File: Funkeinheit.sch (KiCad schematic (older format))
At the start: 3 parts, among them IC1 74HC4050

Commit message: Implements stepup dc/dc
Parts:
- removed IC1: 74HC4050, Housings_SSOP:SSOP-16_5.3x6.2mm_Pitch0.65mm, symbol 74HC4050
- added C10: 220nF, symbol C
- added C11: 100nF, symbol C
- added C12, C13, C7, C8: 150uF, symbol CP
- added C9: 10nF, symbol C
- added D2: D_Schottky, symbol D_Schottky
- added L2: 1uH, symbol L
- added Q1, Q2, Q3, Q4, Q5: Q_NPN_BCE, symbol Q_NPN_BCE
- added Q6: Q_NPN_BCE, TO_SOT_Packages_SMD:TSOT-23_HandSoldering, symbol Q_NPN_BCE
- added R10, R11, R12, R13, R9: 4k7, symbol R
- added R14, R15, R16, R17, R18, R4, R5, R6, R7, R8: 10k, symbol R
- added R19, R20: 100k, symbol R
- added R21: 35k, symbol R
- added R22, R23: 270k, symbol R
- added R24: 2R, symbol R
- added U2: MAX1709, Housings_SSOP:TSSOP-28-1EP_4.4x9.7mm_Pitch0.65mm, symbol MAX1709
- R2: value R -> 10k
- R3: value R -> 4k7
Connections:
- net labels added: +5V, 5V, PGND, ~ENABLE~
- wire segments 13 -> 78
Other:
- note added: "ESR < 15mOhm\nPolymer Capacitor"
- note added: "I > 1.5A\nf = 600kHz"
- note added: "Low ESR Tantal"
- note added: "Pmax > 500mW"

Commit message: Adds new Modules and WDT Circuit
- Added Schematic for MAX892 Highside Switch
- Added Schematic for MC74HC4538A
- Constructed Watchdogtimer Circuit to Reset µC and Radiomodule
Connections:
- wire segments 78 -> 80
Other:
- note added: "Ground Bridge"
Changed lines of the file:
@@
 Text Label 2850 4450 0    60   ~ 0
 MISO
-Text HLabel 2200 4800 3    60   Input ~ 0
-GND
 Text HLabel 2150 1400 0    60   Input ~ 0
 SS
@@
 	1    0    0    -1
 $EndComp
-Text HLabel 10050 1750 2    60   Input ~ 0
-GND
 $Comp
 L CP C13
@@
 	0    1    1    0
 $EndComp
-Text HLabel 5400 950  0    60   Input ~ 0
-+3.3V
 $Comp
 L CP C8
@@
 Wire Wire Line
 	3800 1400 4250 1400
-Text HLabel 8250 3150 3    60   Input ~ 0
-GND
 $Comp
 L R R23
@@
 Wire Wire Line
 	7000 1650 6700 1650
-Text HLabel 6700 2050 3    60   Input ~ 0
-GND
 $Comp
 L R R19
@@
 	1    0    0    -1
 $EndComp
-Text HLabel 6200 2150 3    60   Input ~ 0
-GND
 Wire Wire Line
 	6400 1850 6000 1850
@@
 Wire Wire Line
 	10800 2550 10800 1450
+$Comp
+L GND #PWR?
+U 1 1 59B87665
+P 2200 4800
+F 0 "#PWR?" H 2200 4550 50  0001 C CNN
+F 1 "GND" H 2200 4650 50  0000 C CNN
+F 2 "" H 2200 4800 50  0001 C CNN
+F 3 "" H 2200 4800 50  0001 C CNN
+	1    2200 4800
+	1    0    0    -1
+$EndComp
+$Comp
+L GND #PWR?
+U 1 1 59B876F0
+P 6200 2150
+F 0 "#PWR?" H 6200 1900 50  0001 C CNN
+F 1 "GND" H 6200 2000 50  0000 C CNN
+F 2 "" H 6200 2150 50  0001 C CNN
+F 3 "" H 6200 2150 50  0001 C CNN
+	1    6200 2150
+	1    0    0    -1
+$EndComp
+$Comp
+L GND #PWR?
+U 1 1 59B879C4
+P 6700 2050
+F 0 "#PWR?" H 6700 1800 50  0001 C CNN
+F 1 "GND" H 6700 1900 50  0000 C CNN
+F 2 "" H 6700 2050 50  0001 C CNN
+F 3 "" H 6700 2050 50  0001 C CNN
+	1    6700 2050
+	1    0    0    -1
+$EndComp
+$Comp
+L GND #PWR?
+U 1 1 59B87A4D
+P 8250 3150
+F 0 "#PWR?" H 8250 2900 50  0001 C CNN
+F 1 "GND" H 8250 3000 50  0000 C CNN
+F 2 "" H 8250 3150 50  0001 C CNN
+F 3 "" H 8250 3150 50  0001 C CNN
+	1    8250 3150
+	1    0    0    -1
+$EndComp
+$Comp
+L GND #PWR?
+U 1 1 59B87B99
+P 10050 1750
+F 0 "#PWR?" H 10050 1500 50  0001 C CNN
+F 1 "GND" H 10050 1600 50  0000 C CNN
+F 2 "" H 10050 1750 50  0001 C CNN
+F 3 "" H 10050 1750 50  0001 C CNN
+	1    10050 1750
+	0    -1   -1   0
+$EndComp
+Connection ~ 8250 3150
+$Comp
+L GND #PWR?
+U 1 1 59B89289
+P 4750 3700
+F 0 "#PWR?" H 4750 3450 50  0001 C CNN
+F 1 "GND" H 4750 3550 50  0000 C CNN
+F 2 "" H 4750 3700 50  0001 C CNN
+F 3 "" H 4750 3700 50  0001 C CNN
+	1    4750 3700
+	1    0    0    -1
+$EndComp
+Wire Wire Line
+	4750 3700 4750 3650
+Wire Wire Line
+	4750 3650 5550 3650
+Text Label 5550 3650 0    60   ~ 0
+PGND
+Wire Notes Line
+	4650 3500 4650 3900
+Wire Notes Line
+	4650 3900 5900 3900
+Wire Notes Line
+	5900 3900 5900 3500
+Wire Notes Line
+	5900 3500 4650 3500
+Text Notes 4700 3450 0    60   ~ 0
+Ground Bridge
 $EndSCHEMATC

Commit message: Adds ESD Protection and finalisation of wdt
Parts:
- removed C10: 220nF, symbol C
- removed C11: 100nF, symbol C
- removed C12, C13, C7, C8: 150uF, symbol CP
- removed C9: 10nF, symbol C
- removed D2: D_Schottky, symbol D_Schottky
- removed L2: 1uH, symbol L
- removed Q6: Q_NPN_BCE, TO_SOT_Packages_SMD:TSOT-23_HandSoldering, symbol Q_NPN_BCE
- removed R19, R20: 100k, symbol R
- removed R21: 35k, symbol R
- removed R22, R23: 270k, symbol R
- removed R24: 2R, symbol R
- removed U2: MAX1709, Housings_SSOP:TSSOP-28-1EP_4.4x9.7mm_Pitch0.65mm, symbol MAX1709
- added C? (x2): 47µF, symbol C
- added C?: C, symbol C
- added L?: L, symbol L
- added U?: LTC3113, symbol LTC3113
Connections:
- net labels added: VBAT
- net labels removed: +5V, ~ENABLE~
- wire segments 80 -> 52
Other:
- note removed: "ESR < 15mOhm\nPolymer Capacitor"
- note removed: "I > 1.5A\nf = 600kHz"
- note removed: "Low ESR Tantal"
- note removed: "Pmax > 500mW"

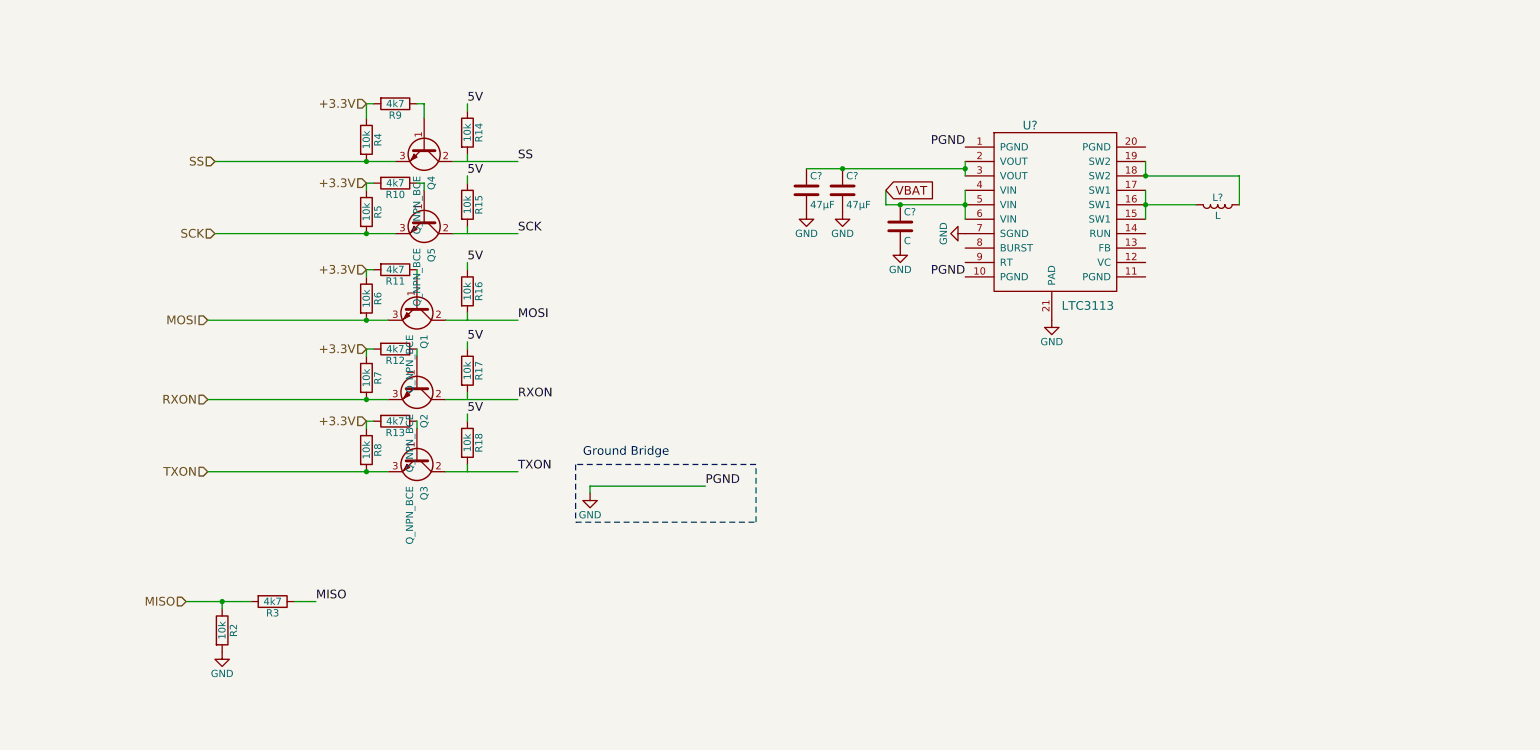
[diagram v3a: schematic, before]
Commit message: Adds RFM23BP Module to Bib and Layout
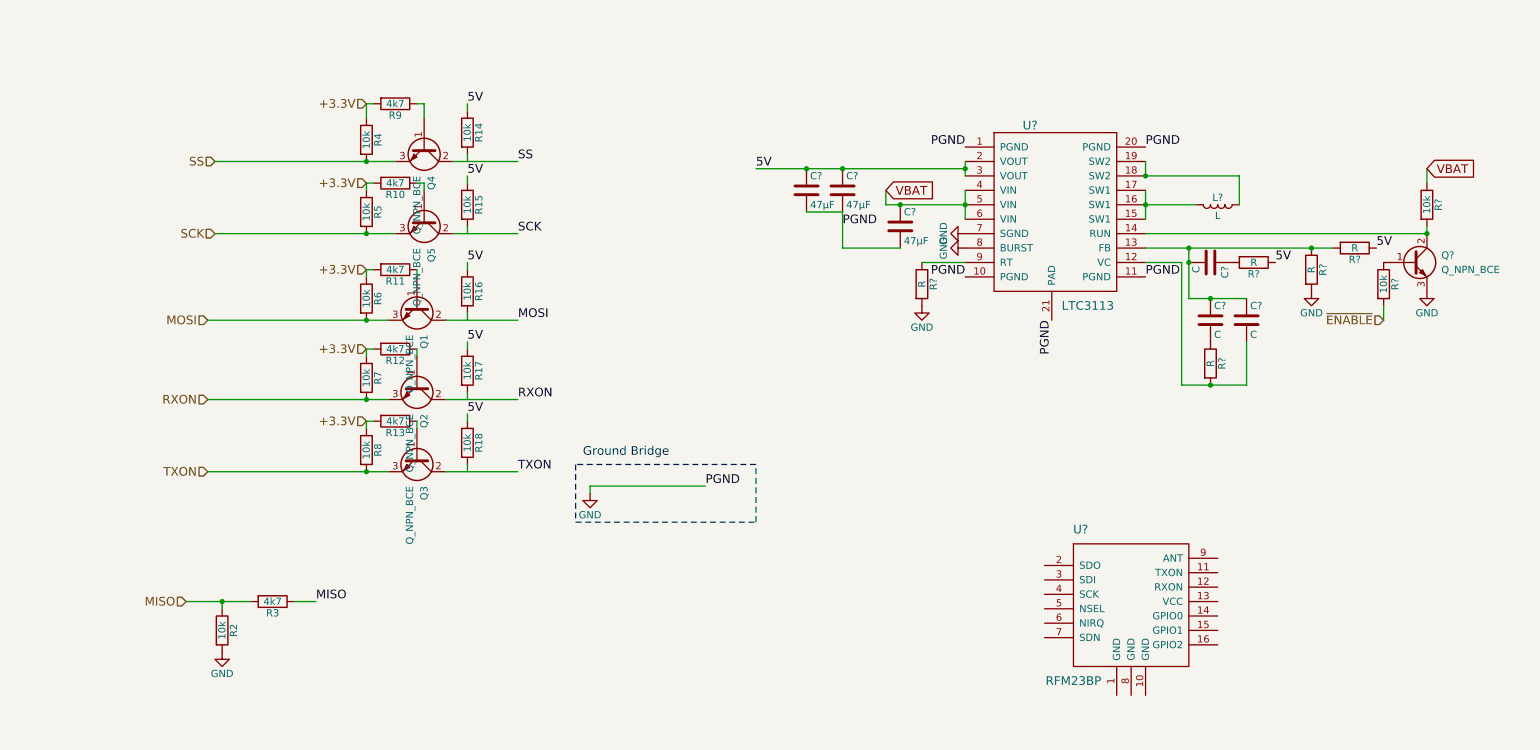
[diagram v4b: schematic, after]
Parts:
- added C? (x3): C, symbol C
- added Q?: Q_NPN_BCE, symbol Q_NPN_BCE
- added R? (x2): 10k, symbol R
- added R? (x5): R, symbol R
- added U?: RFM23BP, symbol RFM23BP
- C?: value C -> 47µF
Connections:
- net labels added: ~ENABLE~
- wire segments 52 -> 67

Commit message: Adds component names
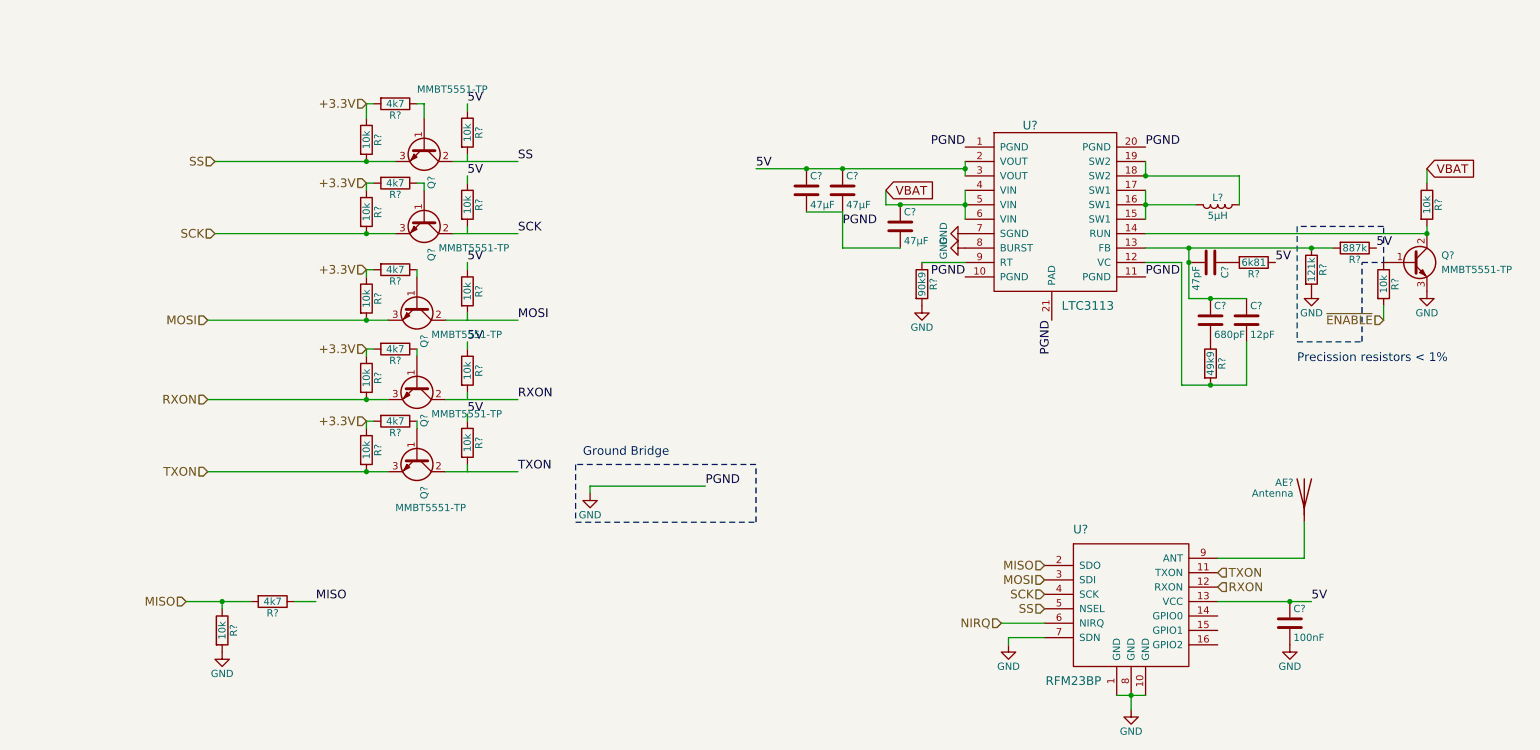
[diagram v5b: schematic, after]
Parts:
- removed C?: C, symbol C
- added AE?: Antenna, symbol Antenna
- added C?: 680pF, Capacitors_SMD:C_0603_HandSoldering, symbol C
- added C?: 100nF, symbol C
- C? (x3): footprint (none) -> Capacitors_SMD:C_1210_HandSoldering
- C?: value C -> 47pF; footprint (none) -> Capacitors_SMD:C_1210_HandSoldering
- C?: value C -> 12pF; footprint (none) -> Capacitors_SMD:C_0603_HandSoldering
- L?: value L -> 5µH
- Q?: renamed from Q4; value Q_NPN_BCE -> MMBT5551-TP
- Q?: renamed from Q5; value Q_NPN_BCE -> MMBT5551-TP
- Q?: renamed from Q1; value Q_NPN_BCE -> MMBT5551-TP
- Q?: renamed from Q2; value Q_NPN_BCE -> MMBT5551-TP
- Q?: renamed from Q3; value Q_NPN_BCE -> MMBT5551-TP
- Q?: value Q_NPN_BCE -> MMBT5551-TP
- R?: renamed from R9; footprint (none) -> Resistors_SMD:R_0603_HandSoldering
- R?: renamed from R4; footprint (none) -> Resistors_SMD:R_0603_HandSoldering
- R?: renamed from R5; footprint (none) -> Resistors_SMD:R_0603_HandSoldering
- R?: renamed from R10; footprint (none) -> Resistors_SMD:R_0603_HandSoldering
- R?: renamed from R6; footprint (none) -> Resistors_SMD:R_0603_HandSoldering
- R?: renamed from R11; footprint (none) -> Resistors_SMD:R_0603_HandSoldering
- R?: renamed from R7; footprint (none) -> Resistors_SMD:R_0603_HandSoldering
- R?: renamed from R12; footprint (none) -> Resistors_SMD:R_0603_HandSoldering
- R?: renamed from R8; footprint (none) -> Resistors_SMD:R_0603_HandSoldering
- R?: renamed from R13; footprint (none) -> Resistors_SMD:R_0603_HandSoldering
- R?: renamed from R14; footprint (none) -> Resistors_SMD:R_0603_HandSoldering
- R?: renamed from R15; footprint (none) -> Resistors_SMD:R_0603_HandSoldering
- R?: renamed from R16; footprint (none) -> Resistors_SMD:R_0603_HandSoldering
- R?: renamed from R17; footprint (none) -> Resistors_SMD:R_0603_HandSoldering
- R?: renamed from R18; footprint (none) -> Resistors_SMD:R_0603_HandSoldering
- R? (x2): footprint (none) -> Resistors_SMD:R_0603_HandSoldering
- R?: value R -> 90k9; footprint (none) -> Resistors_SMD:R_0603_HandSoldering
- R?: value R -> 887k; footprint (none) -> Resistors_SMD:R_0603_HandSoldering
- R?: value R -> 121k; footprint (none) -> Resistors_SMD:R_0603_HandSoldering
- R?: value R -> 6k81; footprint (none) -> Resistors_SMD:R_0603_HandSoldering
- R?: value R -> 49k9; footprint (none) -> Resistors_SMD:R_0603_HandSoldering
- renumbered R2 to R?, R3 to R?
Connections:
- net labels added: NIRQ
- wire segments 67 -> 75
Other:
- note added: "Precission resistors < 1%"

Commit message: Auto stash before merge of "master" and "github/master"
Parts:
- C19: renamed from C?; footprint (none) -> Capacitors_SMD:C_0603_HandSoldering
- L2: renamed from L?; footprint (none) -> Inductors_SMD:L_6.3x6.3_H3; Typ (none) -> CDRH5D28RNP-5R0NC
- Q3, Q4, Q5, Q6, Q7, Q8: renamed from Q?; footprint (none) -> TO_SOT_Packages_SMD:SOT-23
- U4: renamed from U?; footprint (none) -> Housings_SSOP:HTSSOP-20-1EP_4.4x6.5mm_Pitch0.65mm_ThermalPad
- gave numbers to parts that had none: 32

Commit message: Adds Connectors
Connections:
- net labels added: MISO_, MOSI_, RXON_, SCK_, SS_, TXON_
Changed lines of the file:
@@
 LIBS:contrib
 LIBS:valves
+LIBS:nxp-ic
+LIBS:7400-ic
 LIBS:cubesatFunkmodul-cache
 LIBS:funkmodul
@@
 $EndDescr
 Text Label 4250 1400 0    60   ~ 0
-SS
+SS_
 Text Label 4250 1900 0    60   ~ 0
-SCK
+SCK_
 Text Label 4250 2500 0    60   ~ 0
-MOSI
+MOSI_
 $Comp
 L R R19
@@
 $EndComp
 Text Label 2850 4450 0    60   ~ 0
-MISO
+MISO_
 Text HLabel 2150 1400 0    60   Input ~ 0
 SS
@@
 MISO
 Text Label 4250 3050 0    60   ~ 0
-RXON
+RXON_
 Text Label 4250 3550 0    60   ~ 0
-TXON
+TXON_
 Text HLabel 2100 3050 0    60   Input ~ 0
 RXON
@@
 	3800 1400 4250 1400
 $Comp
-L GND #PWR027
+L GND #PWR028
 U 1 1 59B87665
 P 2200 4800
-F 0 "#PWR027" H 2200 4550 50  0001 C CNN
+F 0 "#PWR028" H 2200 4550 50  0001 C CNN
 F 1 "GND" H 2200 4650 50  0000 C CNN
 F 2 "" H 2200 4800 50  0001 C CNN
@@
 $EndComp
 $Comp
-L GND #PWR028
+L GND #PWR029
 U 1 1 59B89289
 P 4750 3700
-F 0 "#PWR028" H 4750 3450 50  0001 C CNN
+F 0 "#PWR029" H 4750 3450 50  0001 C CNN
 F 1 "GND" H 4750 3550 50  0000 C CNN
 F 2 "" H 4750 3700 50  0001 C CNN
@@
 PGND
 $Comp
-L GND #PWR029
+L GND #PWR030
 U 1 1 59BD80CC
 P 7350 1900
-F 0 "#PWR029" H 7350 1650 50  0001 C CNN
+F 0 "#PWR030" H 7350 1650 50  0001 C CNN
 F 1 "GND" H 7350 1750 50  0000 C CNN
 F 2 "" H 7350 1900 50  0001 C CNN
@@
 5V
 $Comp
-L GND #PWR030
+L GND #PWR031
 U 1 1 59C59DAC
 P 7350 2000
-F 0 "#PWR030" H 7350 1750 50  0001 C CNN
+F 0 "#PWR031" H 7350 1750 50  0001 C CNN
 F 1 "GND" H 7350 1850 50  0000 C CNN
 F 2 "" H 7350 2000 50  0001 C CNN
@@
 	10550 1850 10550 1900
 $Comp
-L GND #PWR031
+L GND #PWR032
 U 1 1 59C5A346
 P 10550 2300
-F 0 "#PWR031" H 10550 2050 50  0001 C CNN
+F 0 "#PWR032" H 10550 2050 50  0001 C CNN
 F 1 "GND" H 10550 2150 50  0000 C CNN
 F 2 "" H 10550 2300 50  0001 C CNN
@@
 $EndComp
 $Comp
-L GND #PWR032
+L GND #PWR033
 U 1 1 59C5FB2A
 P 7050 2400
-F 0 "#PWR032" H 7050 2150 50  0001 C CNN
+F 0 "#PWR033" H 7050 2150 50  0001 C CNN
 F 1 "GND" H 7050 2250 50  0000 C CNN
 F 2 "" H 7050 2400 50  0001 C CNN
@@
 $EndComp
 $Comp
-L GND #PWR033
+L GND #PWR034
 U 1 1 59C6029F
 P 9750 2300
-F 0 "#PWR033" H 9750 2050 50  0001 C CNN
+F 0 "#PWR034" H 9750 2050 50  0001 C CNN
 F 1 "GND" H 9750 2150 50  0000 C CNN
 F 2 "" H 9750 2300 50  0001 C CNN
@@
 Text Label 9750 4450 0    60   ~ 0
 5V
-Text HLabel 9100 4250 2    60   Input ~ 0
-TXON
-Text HLabel 9100 4350 2    60   Input ~ 0
-RXON
 $Comp
 L Antenna AE1
@@
 	9700 4150 9700 3900
 $Comp
-L GND #PWR034
+L GND #PWR035
 U 1 1 59C98D82
 P 8500 5200
-F 0 "#PWR034" H 8500 4950 50  0001 C CNN
+F 0 "#PWR035" H 8500 4950 50  0001 C CNN
 F 1 "GND" H 8500 5050 50  0000 C CNN
 F 2 "" H 8500 5200 50  0001 C CNN
@@
 	8500 5100 8500 5200
 Connection ~ 8500 5100
-Text HLabel 7900 4500 0    60   Input ~ 0
-SS
-Text HLabel 7900 4400 0    60   Input ~ 0
-SCK
-Text HLabel 7900 4300 0    60   Input ~ 0
-MOSI
-Text HLabel 7900 4200 0    60   Input ~ 0
-MISO
-$Comp
-L GND #PWR035
+$Comp
+L GND #PWR036
 U 1 1 59C9947D
 P 7650 4750
-F 0 "#PWR035" H 7650 4500 50  0001 C CNN
+F 0 "#PWR036" H 7650 4500 50  0001 C CNN
 F 1 "GND" H 7650 4600 50  0000 C CNN
 F 2 "" H 7650 4750 50  0001 C CNN
@@
 $EndComp
 $Comp
-L GND #PWR036
+L GND #PWR037
 U 1 1 59CB2BA8
 P 9600 4750
-F 0 "#PWR036" H 9600 4500 50  0001 C CNN
+F 0 "#PWR037" H 9600 4500 50  0001 C CNN
 F 1 "GND" H 9600 4600 50  0000 C CNN
 F 2 "" H 9600 4750 50  0001 C CNN
@@
 $EndComp
 Connection ~ 9600 4450
+Connection ~ 3900 1400
+Connection ~ 3900 1900
+Connection ~ 3900 2500
+Connection ~ 3900 3050
+Connection ~ 3900 3550
+Text Label 7900 4500 2    60   ~ 0
+SS_
+Text Label 7900 4400 2    60   ~ 0
+SCK_
+Text Label 7900 4300 2    60   ~ 0
+MOSI_
+Text Label 7900 4200 2    60   ~ 0
+MISO_
+Text Label 9100 4250 0    60   ~ 0
+TXON_
+Text Label 9100 4350 0    60   ~ 0
+RXON_
 $EndSCHEMATC
